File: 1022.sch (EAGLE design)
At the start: 10 parts, among them J2 HR911105A, U1 HLK-RM04, U2 I2C-24C64

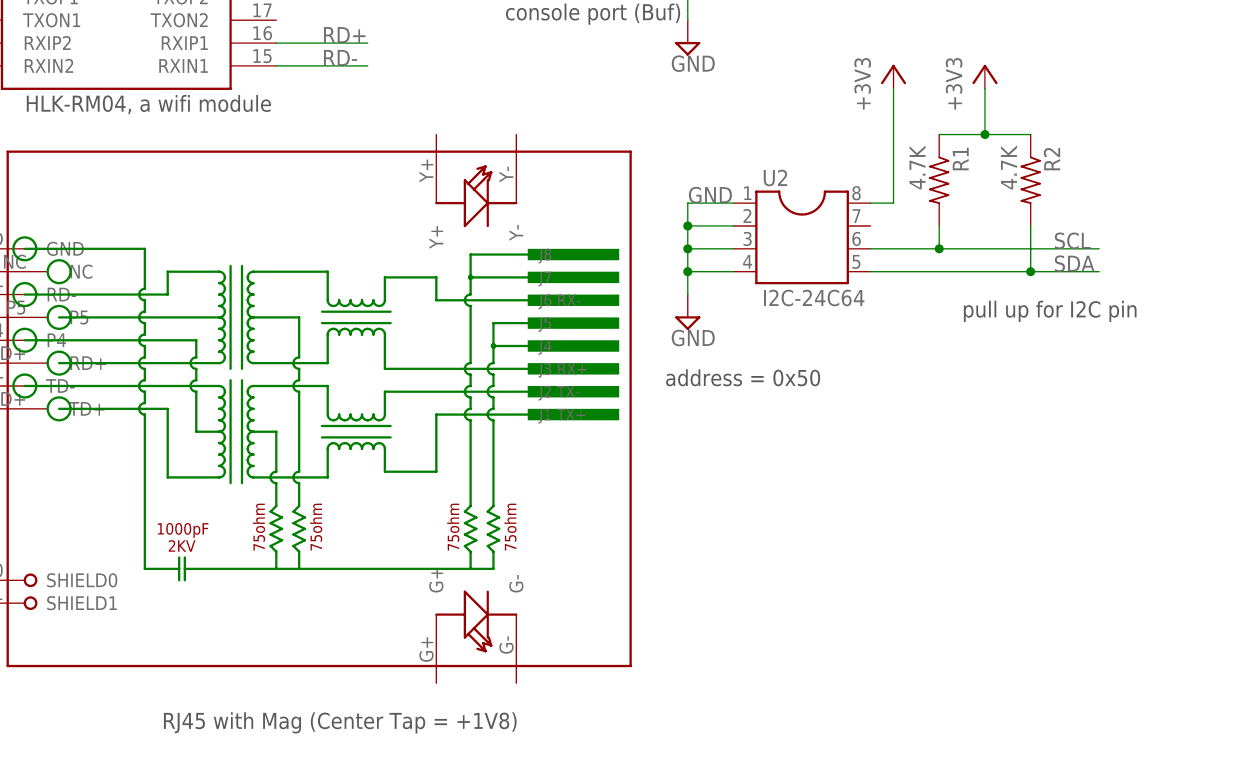
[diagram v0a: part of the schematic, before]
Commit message: add I2C MCU TI MSP430G2553
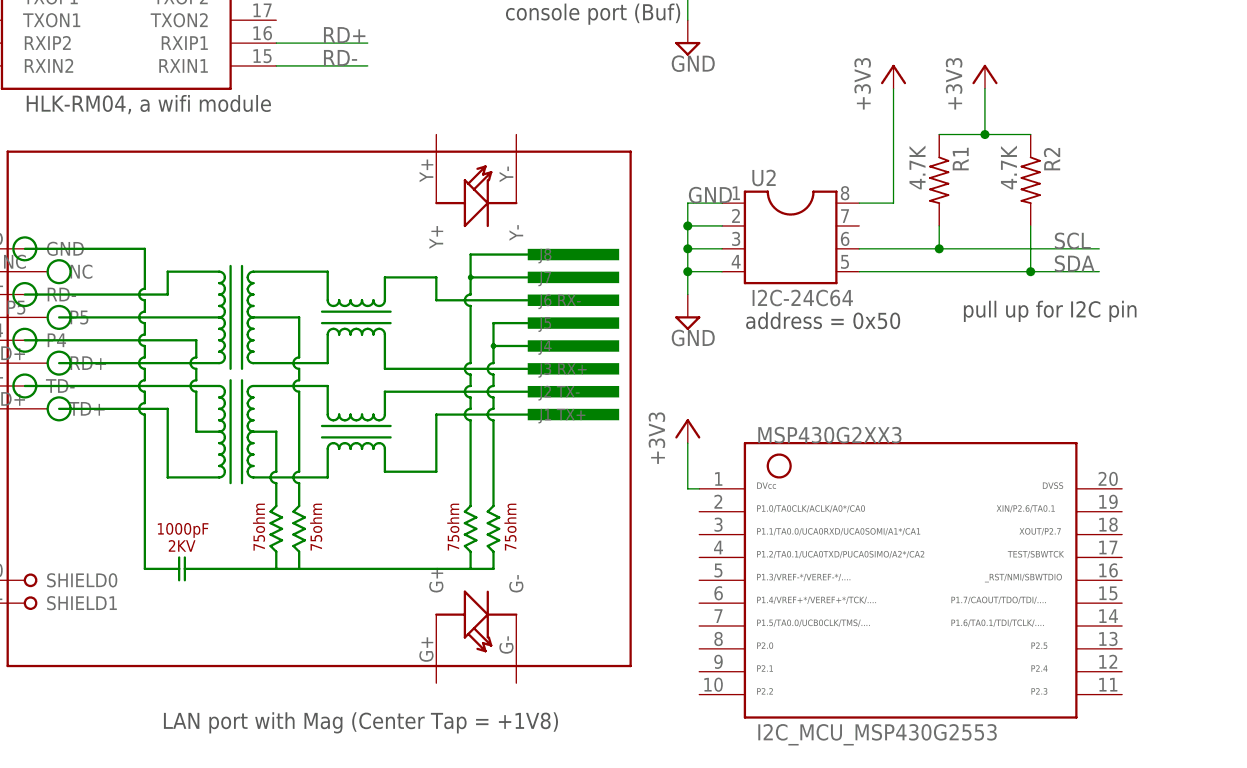
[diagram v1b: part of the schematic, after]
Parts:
- added I2C_MCU_MSP430G2553: G2XX3---N20, TI_MSP430_v16:G2XX3---N20
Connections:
- net +3V3: now also I2C_MCU_MSP430G2553.1
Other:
- note added: "LAN port with Mag (Center Tap = +1V8)"
- note removed: "RJ45 with Mag (Center Tap = +1V8)"
- moved on the sheet: U2

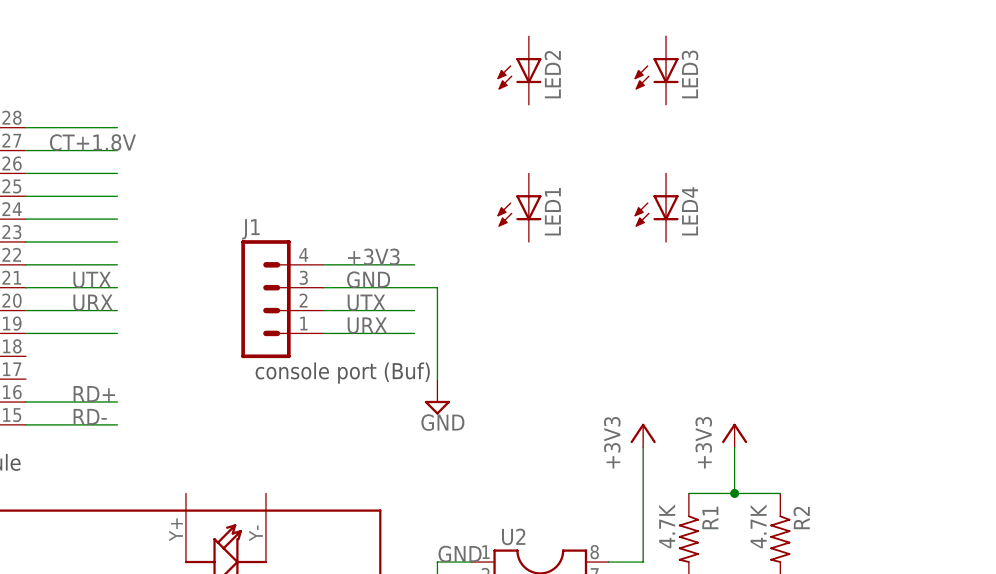
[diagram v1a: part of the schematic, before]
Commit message: add USB MicroB conn
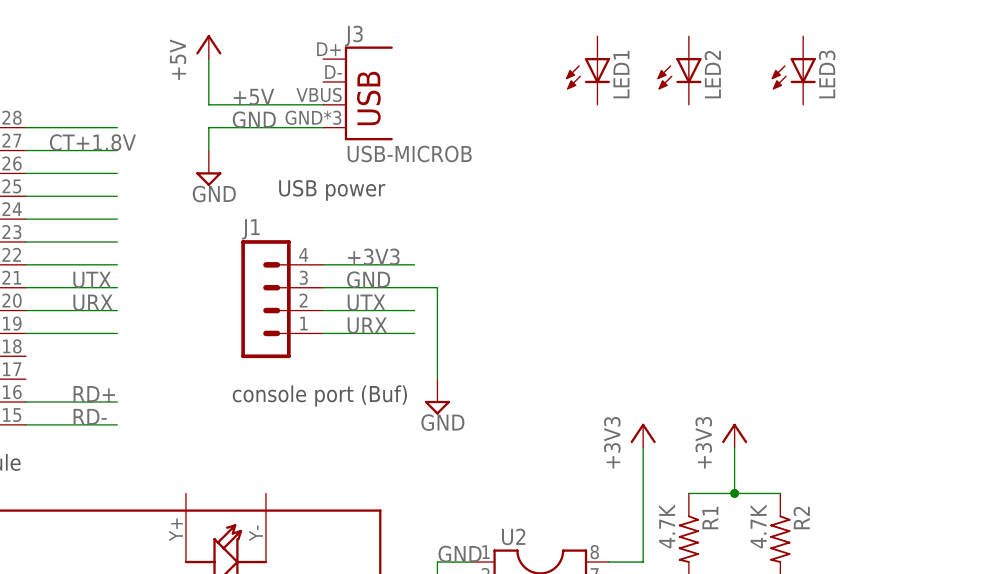
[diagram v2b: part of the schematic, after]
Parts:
- removed LED4: (no value), led:LED3MM
- added J3: USB-MICROB, clavis-eagle-pcb-build:USB-MICROB
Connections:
- net +5V: now also J3.VBUS
- net GND: now also J3.GND
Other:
- note added: "USB power"
- moved on the sheet: LED1, LED2, LED3
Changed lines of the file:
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@@
 <setting verticaltext="up"/>
 </settings>
-<grid distance="1.27" unitdist="mm" unit="mm" style="lines" multiple="1" display="yes" altdistance="0.01" altunitdist="inch" altunit="inch"/>
+<grid distance="0.1" unitdist="inch" unit="inch" style="lines" multiple="1" display="no" altdistance="0.01" altunitdist="inch" altunit="inch"/>
 <layers>
-<layer number="1" name="Top" color="4" fill="1" visible="yes" active="no"/>
-<layer number="16" name="Bottom" color="1" fill="1" visible="yes" active="no"/>
-<layer number="17" name="Pads" color="2" fill="1" visible="yes" active="no"/>
-<layer number="18" name="Vias" color="2" fill="1" visible="yes" active="no"/>
-<layer number="19" name="Unrouted" color="6" fill="1" visible="yes" active="no"/>
-<layer number="20" name="Dimension" color="15" fill="1" visible="yes" active="no"/>
-<layer number="21" name="tPlace" color="7" fill="1" visible="yes" active="no"/>
-<layer number="22" name="bPlace" color="7" fill="1" visible="yes" active="no"/>
-<layer number="23" name="tOrigins" color="15" fill="1" visible="yes" active="no"/>
-<layer number="24" name="bOrigins" color="15" fill="1" visible="yes" active="no"/>
-<layer number="25" name="tNames" color="7" fill="1" visible="yes" active="no"/>
-<layer number="26" name="bNames" color="7" fill="1" visible="yes" active="no"/>
-<layer number="27" name="tValues" color="7" fill="1" visible="yes" active="no"/>
-<layer number="28" name="bValues" color="7" fill="1" visible="yes" active="no"/>
+<layer number="1" name="Top" color="4" fill="1" visible="no" active="no"/>
+<layer number="16" name="Bottom" color="1" fill="1" visible="no" active="no"/>
+<layer number="17" name="Pads" color="2" fill="1" visible="no" active="no"/>
+<layer number="18" name="Vias" color="2" fill="1" visible="no" active="no"/>
+<layer number="19" name="Unrouted" color="6" fill="1" visible="no" active="no"/>
+<layer number="20" name="Dimension" color="15" fill="1" visible="no" active="no"/>
+<layer number="21" name="tPlace" color="7" fill="1" visible="no" active="no"/>
+<layer number="22" name="bPlace" color="7" fill="1" visible="no" active="no"/>
+<layer number="23" name="tOrigins" color="15" fill="1" visible="no" active="no"/>
+<layer number="24" name="bOrigins" color="15" fill="1" visible="no" active="no"/>
+<layer number="25" name="tNames" color="7" fill="1" visible="no" active="no"/>
+<layer number="26" name="bNames" color="7" fill="1" visible="no" active="no"/>
+<layer number="27" name="tValues" color="7" fill="1" visible="no" active="no"/>
+<layer number="28" name="bValues" color="7" fill="1" visible="no" active="no"/>
 <layer number="29" name="tStop" color="7" fill="3" visible="no" active="no"/>
 <layer number="30" name="bStop" color="7" fill="6" visible="no" active="no"/>
@@
 <layer number="35" name="tGlue" color="7" fill="4" visible="no" active="no"/>
 <layer number="36" name="bGlue" color="7" fill="5" visible="no" active="no"/>
-<layer number="37" name="tTest" color="7" fill="1" visible="yes" active="no"/>
-<layer number="38" name="bTest" color="7" fill="1" visible="yes" active="no"/>
+<layer number="37" name="tTest" color="7" fill="1" visible="no" active="no"/>
+<layer number="38" name="bTest" color="7" fill="1" visible="no" active="no"/>
 <layer number="39" name="tKeepout" color="4" fill="11" visible="no" active="no"/>
 <layer number="40" name="bKeepout" color="1" fill="11" visible="no" active="no"/>
@@
 <layer number="44" name="Drills" color="7" fill="1" visible="no" active="no"/>
 <layer number="45" name="Holes" color="7" fill="1" visible="no" active="no"/>
-<layer number="46" name="Milling" color="3" fill="1" visible="yes" active="no"/>
-<layer number="47" name="Measures" color="7" fill="1" visible="yes" active="no"/>
-<layer number="48" name="Document" color="7" fill="1" visible="yes" active="no"/>
-<layer number="49" name="Reference" color="7" fill="1" visible="yes" active="no"/>
-<layer number="50" name="dxf" color="7" fill="1" visible="yes" active="no"/>
-<layer number="51" name="tDocu" color="7" fill="1" visible="yes" active="no"/>
-<layer number="52" name="bDocu" color="7" fill="1" visible="yes" active="no"/>
-<layer number="53" name="tGND_GNDA" color="7" fill="9" visible="yes" active="no"/>
-<layer number="54" name="bGND_GNDA" color="1" fill="9" visible="yes" active="no"/>
-<layer number="56" name="wert" color="7" fill="1" visible="yes" active="no"/>
-<layer number="57" name="tCAD" color="7" fill="1" visible="yes" active="no"/>
-<layer number="59" name="tCarbon" color="7" fill="1" visible="yes" active="no"/>
-<layer number="60" name="bCarbon" color="7" fill="1" visible="yes" active="no"/>
+<layer number="46" name="Milling" color="3" fill="1" visible="no" active="no"/>
+<layer number="47" name="Measures" color="7" fill="1" visible="no" active="no"/>
+<layer number="48" name="Document" color="7" fill="1" visible="no" active="no"/>
+<layer number="49" name="Reference" color="7" fill="1" visible="no" active="no"/>
+<layer number="50" name="dxf" color="7" fill="1" visible="no" active="no"/>
+<layer number="51" name="tDocu" color="7" fill="1" visible="no" active="no"/>
+<layer number="52" name="bDocu" color="7" fill="1" visible="no" active="no"/>
+<layer number="53" name="tGND_GNDA" color="7" fill="9" visible="no" active="no"/>
+<layer number="54" name="bGND_GNDA" color="1" fill="9" visible="no" active="no"/>
+<layer number="56" name="wert" color="7" fill="1" visible="no" active="no"/>
+<layer number="57" name="tCAD" color="7" fill="1" visible="no" active="no"/>
+<layer number="59" name="tCarbon" color="7" fill="1" visible="no" active="no"/>
+<layer number="60" name="bCarbon" color="7" fill="1" visible="no" active="no"/>
 <layer number="90" name="Modules" color="5" fill="1" visible="yes" active="yes"/>
 <layer number="91" name="Nets" color="2" fill="1" visible="yes" active="yes"/>
@@
 <part name="LED2" library="led" deviceset="LED" device="3MM"/>
 <part name="LED3" library="led" deviceset="LED" device="3MM"/>
-<part name="LED4" library="led" deviceset="LED" device="3MM"/>
 <part name="J1" library="con-lstb" deviceset="MA04-1" device=""/>
 <part name="SUPPLY2" library="supply2" deviceset="GND" device=""/>
@@
 <part name="I2C_MCU_MSP430G2553" library="TI_MSP430_v16" deviceset="G2XX3---N20" device=""/>
 <part name="+3V3" library="supply1" deviceset="+3V3" device=""/>
+<part name="J3" library="clavis-eagle-pcb-build" deviceset="USB" device="-MICROB"/>
+<part name="SUPPLY5" library="supply2" deviceset="GND" device=""/>
+<part name="P+1" library="supply1" deviceset="+5V" device=""/>
 </parts>
 <sheets>
@@
 <plain>
 <text x="12.7" y="43.18" size="1.778" layer="97">HLK-RM04, a wifi module</text>
-<text x="66.04" y="53.34" size="1.778" layer="97">console port (Buf)</text>
+<text x="63.5" y="50.8" size="1.778" layer="97">console port (Buf)</text>
 <text x="116.84" y="20.32" size="1.778" layer="97">pull up for I2C pin</text>
 <text x="27.94" y="-25.4" size="1.778" layer="97">LAN port with Mag (Center Tap = +1V8)</text>
 <text x="92.71" y="19.05" size="1.778" layer="97">address = 0x50</text>
+<text x="68.58" y="73.66" size="1.778" layer="97">USB power</text>
 </plain>
 <instances>
@@
 <instance part="SUPPLY1" gate="GND" x="-12.7" y="71.12"/>
 <instance part="U2" gate="G$1" x="97.79" y="30.48"/>
-<instance part="LED1" gate="G$1" x="96.52" y="73.66"/>
-<instance part="LED2" gate="G$1" x="96.52" y="88.9"/>
-<instance part="LED3" gate="G$1" x="111.76" y="88.9"/>
-<instance part="LED4" gate="G$1" x="111.76" y="73.66"/>
+<instance part="LED1" gate="G$1" x="104.14" y="88.9"/>
+<instance part="LED2" gate="G$1" x="114.3" y="88.9"/>
+<instance part="LED3" gate="G$1" x="127" y="88.9"/>
 <instance part="J1" gate="1" x="66.04" y="63.5"/>
 <instance part="SUPPLY2" gate="GND" x="86.36" y="50.8"/>
@@
 <instance part="I2C_MCU_MSP430G2553" gate="G$1" x="111.76" y="-6.35"/>
 <instance part="+3V3" gate="G$1" x="86.36" y="8.89"/>
+<instance part="J3" gate="G$1" x="76.2" y="81.28"/>
+<instance part="SUPPLY5" gate="GND" x="60.96" y="76.2"/>
+<instance part="P+1" gate="1" x="60.96" y="91.44"/>
 </instances>
 <busses>
@@
 <label x="86.36" y="33.02" size="1.778" layer="95"/>
 </segment>
+<segment>
+<pinref part="J3" gate="G$1" pin="GND"/>
+<pinref part="SUPPLY5" gate="GND" pin="GND"/>
+<wire x1="73.66" y1="81.28" x2="60.96" y2="81.28" width="0.1524" layer="91"/>
+<wire x1="60.96" y1="81.28" x2="60.96" y2="78.74" width="0.1524" layer="91"/>
+<label x="63.5" y="81.28" size="1.778" layer="95"/>
+</segment>
 </net>
 <net name="+5V" class="0">
@@
 <label x="-5.08" y="81.28" size="1.778" layer="95"/>
 </segment>
-</net>
+<segment>
+<pinref part="J3" gate="G$1" pin="VBUS"/>
+<pinref part="P+1" gate="1" pin="+5V"/>
+<wire x1="73.66" y1="83.82" x2="60.96" y2="83.82" width="0.1524" layer="91"/>
+<wire x1="60.96" y1="83.82" x2="60.96" y2="88.9" width="0.1524" layer="91"/>
+<label x="63.5" y="83.82" size="1.778" layer="95"/>
+</segment>
+</net>
